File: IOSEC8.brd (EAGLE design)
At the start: 133 x 40 mm, 44 parts

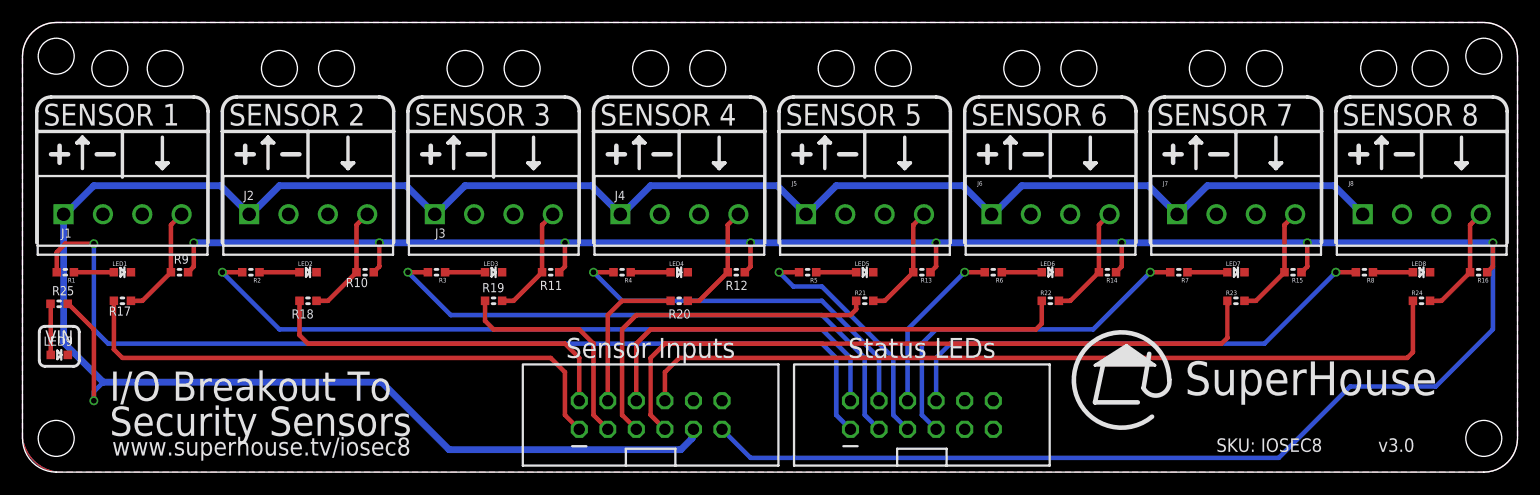
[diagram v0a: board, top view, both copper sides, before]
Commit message: Massive update to reduce PCB size for v4.0 release
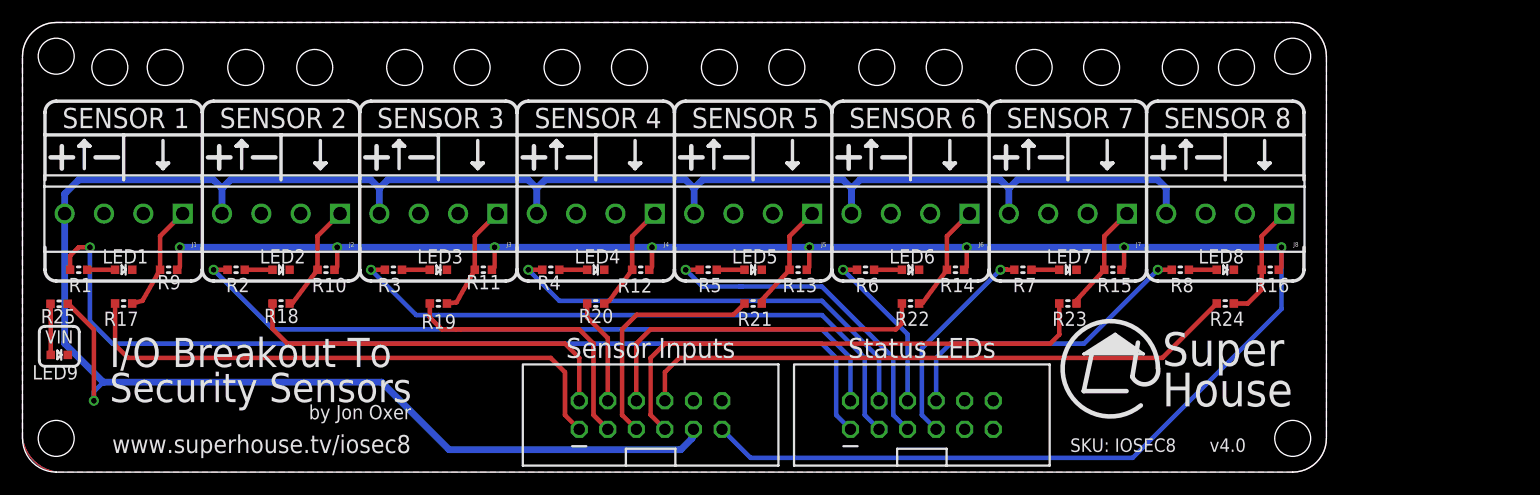
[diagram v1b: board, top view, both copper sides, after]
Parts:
- removed JP1, JP2: M06X2, freetronics-jon:2X6-SHROUDED
- added J10, J9: M02X6-SHROUDED, SuperHouse-Connectors:2X06-SHROUDED
- J1, J2, J3, J4, J5, J6, J7, J8: device freetronics-master-v1.1:SCREWTERMINAL-3.5MM-4 -> SuperHouse-Connectors:SCREWTERMINAL-3.5MM-4
- LED1, LED2, LED3, LED4, LED5, LED6, LED7, LED8, LED9: device freetronics-jon:LED-0603 -> SuperHouse-LEDs:LED-0603
- R1, R10, R11, R12, R13, R14, R15, R16, R17, R18, R19, R2, R20, R21, R22, R23, R24, R25, R3, R4, R5, R6, R7, R8, R9: device freetronics-jon:0603 -> SuperHouse-DiscreteSemi:R0603
- moved R16 18.5 mm to (111.0, 18.0)
- moved R24 17.5 mm to (107.0, 15.0)
- moved LED8 17.5 mm to (107.0, 18.0)
- moved R8 16.4 mm to (103.0, 18.0)
- moved R15 16.0 mm to (97.0, 18.0)
- moved R23 15.0 mm to (93.0, 15.0)
- moved LED7 15.0 mm to (93.0, 18.0)
- moved R7 13.9 mm to (89.0, 18.0)
- moved R14 13.5 mm to (83.0, 18.0)
- moved R22 12.4 mm to (79.0, 15.0)
- moved LED6 12.4 mm to (79.0, 18.0)
- moved J8 12.2 mm to (107.0, 23.0), turned to 180 degrees
- moved R6 11.4 mm to (75.0, 18.0)
- moved R13 11.0 mm to (69.0, 18.0)
- moved R21 9.93 mm to (65.0, 15.0)
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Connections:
- net GND: now also J10.10, J9.10; no longer JP1.10, JP2.10
- net IO1: now also J9.1; no longer JP1.1
- net IO2: now also J9.2; no longer JP1.2
- net IO3: now also J9.3; no longer JP1.3
- net IO4: now also J9.4; no longer JP1.4
- net IO5: now also J9.5; no longer JP1.5
- net IO6: now also J9.6; no longer JP1.6
- net IO7: now also J9.7; no longer JP1.7
- net IO8: now also J9.8; no longer JP1.8
- net IOREF: now also J9.11; no longer JP1.11
- net L1: now also J10.1; no longer JP2.1
- net L2: now also J10.2; no longer JP2.2
- net L3: now also J10.3; no longer JP2.3
- net L4: now also J10.4; no longer JP2.4
- net L5: now also J10.5; no longer JP2.5
- net L6: now also J10.6; no longer JP2.6
- net L7: now also J10.7; no longer JP2.7
- net L8: now also J10.8; no longer JP2.8
- net N$10: now also J8.1; no longer J8.4
- net N$249: now also J3.1; no longer J3.4
- net N$256: now also J4.1; no longer J4.4
- net N$262: now also J1.1; no longer J1.4
- net N$3: now also J2.1; no longer J2.4
- net N$7: now also J5.1; no longer J5.4
- net N$8: now also J6.1; no longer J6.4
- net N$9: now also J7.1; no longer J7.4
- net RESET: now also J9.12; no longer JP1.12
- net VIN: now also J1.4, J2.4, J3.4, J4.4, J5.4, J6.4, J7.4, J8.4, J9.9; no longer J1.1, J2.1, J3.1, J4.1, J5.1, J6.1, J7.1, J8.1, JP1.9
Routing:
- net IOREF: track 220.3 -> 176.6 mm
- net IO8: track 74.4 -> 54.2 mm
- net L8: track 44.3 -> 28.0 mm
- net IO7: track 62.2 -> 46.9 mm
- net L7: track 32.9 -> 18.8 mm
- net IO6: track 43.9 -> 31.2 mm
- net IO5: track 31.7 -> 21.3 mm
- net VIN: track 214.5 -> 204.3 mm
- net L5: track 22.0 -> 29.8 mm
- net L4: track 34.1 -> 39.5 mm
- net IO3: track 20.4 -> 24.9 mm
- net IO4: track 13.7 -> 9.41 mm
- net L3: track 52.5 -> 55.3 mm
- net L1: track 87.0 -> 84.5 mm
- net IO2: track 32.6 -> 34.4 mm
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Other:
- board size 133 x 40 mm -> 116 x 40 mm
- board text added: "(c) 2017-2019 SuperHouse Automation Pty Ltd"
- board text added: "Super House"
- board text added: "by Jon Oxer"
- board text added: "v4.0"
- board text removed: "(c) 2018 SuperHouse Automation Pty Ltd"
- board text removed: "SuperHouse"
- board text removed: "v3.0"
